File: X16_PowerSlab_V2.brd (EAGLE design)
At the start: 152.4 x 76.2 mm, 45 parts, among them J1 CONN_796636-3, J2 CONN_796636-3, J3 CONN_ET60T

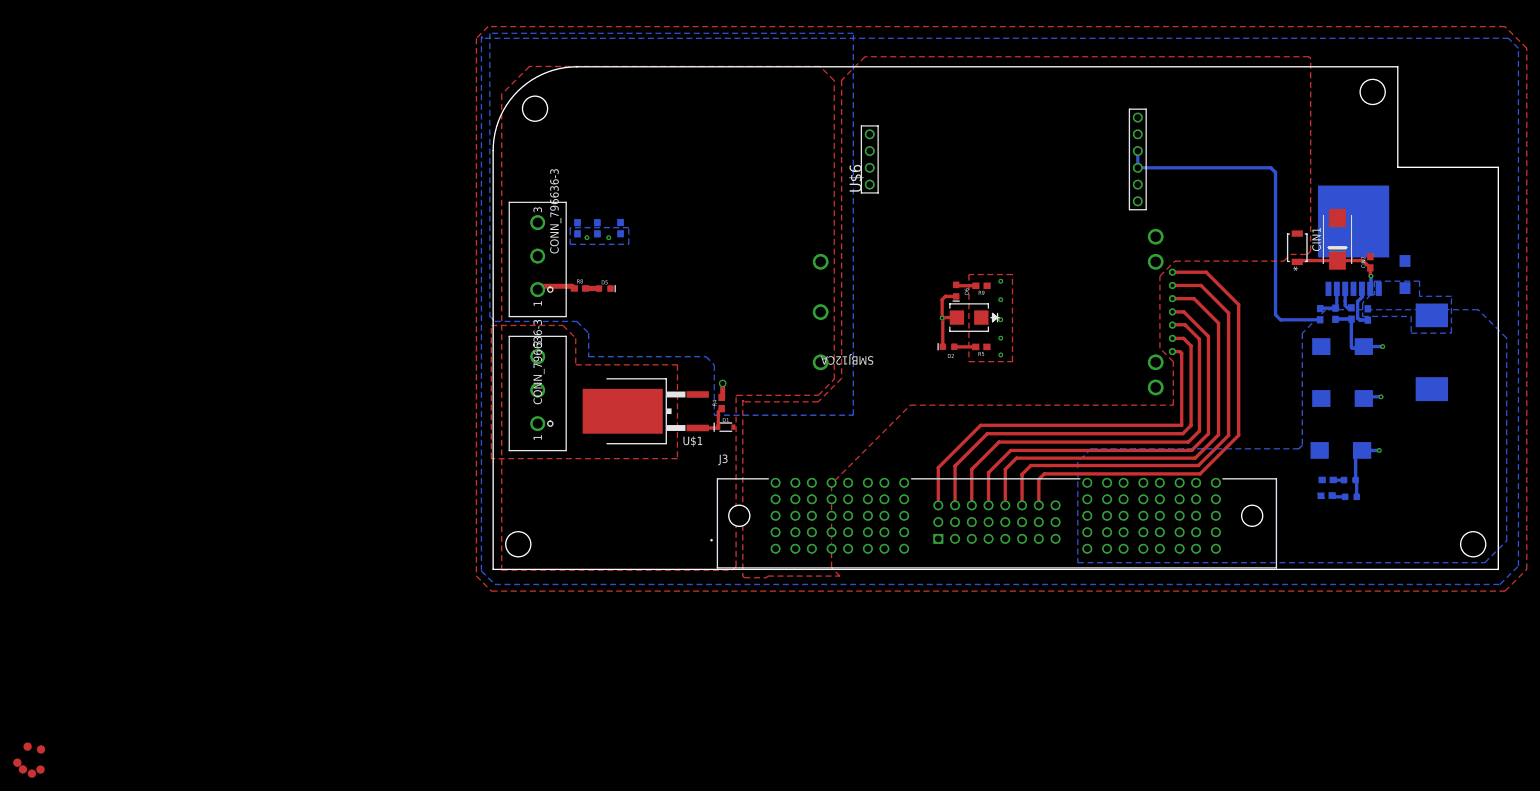
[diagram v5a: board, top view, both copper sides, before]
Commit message: Followed video, few discrepancies
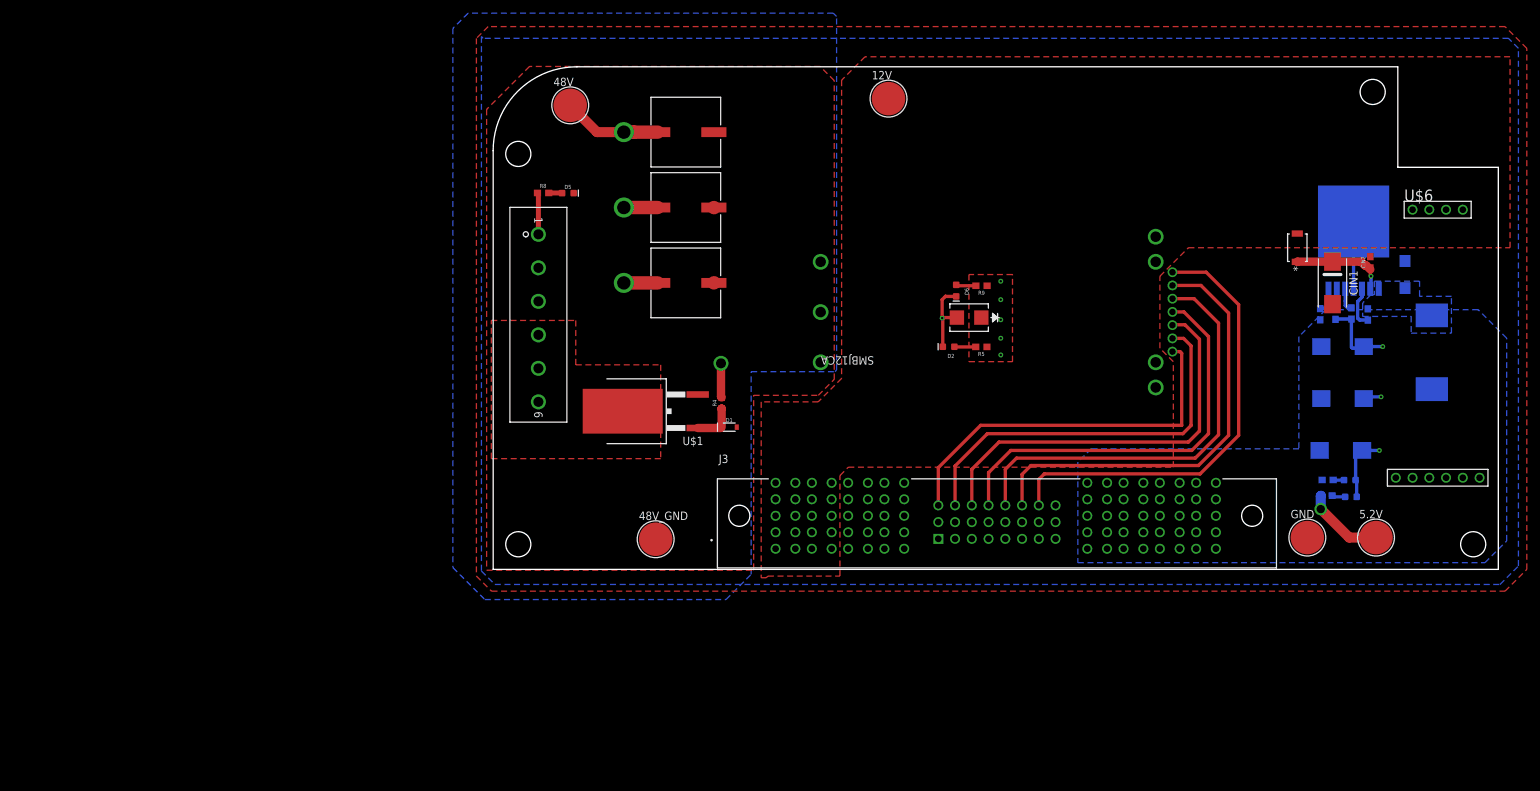
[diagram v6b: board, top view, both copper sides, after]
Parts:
- removed 12VGND_TP, 12V_TP, 48VGND_TP, 48_TP, TP5, TP6: TEST-POINT3X5, SparkFun-Connectors:PAD.03X.05
- removed C3, C4, C7: 330uF, SparkFun-Capacitors:0603-POLAR
- removed J1, J2: CONN_796636-3, X16_Power_Slab:CONN_796636-3
- added 12V, 48V_GND, 5.2V, GND: TESTPOINT_5.04MM, X16-ExtraComponents:TESTPOINT_5.04MM
- added 48V: 48V, X16-ExtraComponents:TESTPOINT_5.04MM
- added C1, C5, C6: UCM1H331MNL1GS, X16_Power_Slab:CAP_UCD_10X10_NCH
- added J4: 796636-6, X16_Power_Slab:CON6_P5MM_VER_TERM-BLK_TYC
- D1: value 15V -> 3.6V
- R1: value 1k -> (none)
- R10: value 100 -> 0.1
- R2: value 3.32k -> (none)
- R4: value 1M -> (none)
- R5: value 600 -> (none)
- R6: value 300 -> (none)
- R8: value 1.5k -> 0.1
- R9: value 470 -> 0.1
- RADJ: value 12.4k -> (none)
- moved U$6 71.5 mm to (143.2, 34.2), turned to 0 degrees
- moved D5 15.5 mm to (11.3, 57.0)
- moved R8 15.5 mm to (7.57, 57.1)
- moved H2 7.31 mm to (3.81, 63.0)
- moved CIN1 6.65 mm to (127.3, 43.4), turned to 270 degrees
- moved D1 0.51 mm to (35.8, 21.6)
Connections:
- net 12V: now also 12V.TP, J3.08, J3.16, J3.24
- net 48V: now also 48V.TP, C1.1, C5.1, C6.1, J4.1, J4.2, J4.3; no longer C3.+, C4.+, C7.+, J1.1, J1.2, J1.3
- net 48V_GND: now also 48V_GND.TP, C1.2, C5.2, C6.2; no longer C3.-, C4.-, C7.-
- net 5.2V: now also 5.2V.TP
- net GND: now also GND.TP
- net GND_RAW: now also J4.4, J4.5, J4.6; no longer J2.1, J2.2, J2.3
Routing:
- net 5.2V: track 52.4 -> 12.2 mm, vias 0 -> 1
- net 48V: track 8.16 -> 38.3 mm, vias 1 -> 4
- net GND: track 36.2 -> 46.4 mm
- net 48V_GND: track 0.00 -> 0.07 mm, vias 2 -> 0
- removed copper zone on layer 16, net 48V_GND

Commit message: Board finished; ran DRC
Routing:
- net 12V: track 0.00 -> 84.9 mm
- net GND: track 46.4 -> 51.8 mm, vias 4 -> 5
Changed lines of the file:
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@@
 <wire x1="130.4544" y1="42.545" x2="130.4544" y2="52.74" width="0.508" layer="16"/>
 <contactref element="GND" pad="TP"/>
+<wire x1="127.254" y1="40.214" x2="122.092" y2="40.214" width="1.016" layer="1"/>
+<wire x1="122.092" y1="40.214" x2="121.92" y2="40.386" width="1.016" layer="1"/>
+<via x="121.92" y="40.386" extent="1-16" drill="1.27"/>
 </signal>
 <signal name="N$1">
@@
 <contactref element="C5" pad="2"/>
 <contactref element="C1" pad="2"/>
-<wire x1="33.4645" y1="43.434" x2="33.48990625" y2="43.45940625" width="2.032" layer="1"/>
-<wire x1="33.4645" y1="54.864" x2="33.4899" y2="54.8386" width="2.032" layer="1"/>
 <contactref element="48V_GND" pad="TP"/>
-<wire x1="33.48990625" y1="43.45940625" x2="49.653" y2="46.632" width="0" layer="19" extent="1-1"/>
-<wire x1="33.4899" y1="54.8386" x2="33.48990625" y2="43.45940625" width="0" layer="19" extent="1-1"/>
-<wire x1="33.4645" y1="66.294" x2="33.4645" y2="54.864" width="0" layer="19" extent="1-1"/>
 </signal>
 <signal name="N$7">
@@
 <contactref element="R10" pad="2"/>
 <contactref element="D7" pad="A"/>
-<wire x1="129.171" y1="11.05493125" x2="129.171" y2="10.9982" width="0.762" layer="16"/>
 <wire x1="127.21498125" y1="11.18193125" x2="127.3987125" y2="10.9982" width="0.508" layer="16"/>
 <wire x1="127.3987125" y1="10.9982" x2="129.171" y2="10.9982" width="0.508" layer="16"/>
@@
 <contactref element="J3" pad="16"/>
 <contactref element="12V" pad="TP"/>
-<wire x1="85.27" y1="7.168" x2="85.27" y2="9.708" width="0" layer="19" extent="1-1"/>
-<wire x1="85.27" y1="4.628" x2="85.27" y2="7.168" width="0" layer="19" extent="1-1"/>
-<wire x1="100.453" y1="27.582" x2="85.27" y2="9.708" width="0" layer="19" extent="1-1"/>
+<wire x1="85.27" y1="4.628" x2="85.27" y2="3.104" width="1.016" layer="1"/>
+<wire x1="85.27" y1="3.104" x2="84.452" y2="2.286" width="1.016" layer="1"/>
+<wire x1="84.452" y1="2.286" x2="66.294" y2="2.286" width="1.016" layer="1"/>
+<wire x1="66.294" y1="2.286" x2="65.024" y2="3.556" width="1.016" layer="1"/>
+<wire x1="68.984" y1="27.582" x2="100.453" y2="27.582" width="1.016" layer="1"/>
+<wire x1="65.024" y1="3.556" x2="65.024" y2="23.622" width="1.016" layer="1"/>
+<wire x1="65.024" y1="23.622" x2="68.984" y2="27.582" width="1.016" layer="1"/>
+<wire x1="85.27" y1="9.708" x2="85.27" y2="7.168" width="1.016" layer="1"/>
+<wire x1="85.27" y1="7.168" x2="85.27" y2="4.628" width="1.016" layer="1"/>
 </signal>
 <signal name="5.2V">
@@
 <contactref element="CIN1" pad="+"/>
 <contactref element="CR2" pad="1"/>
-<wire x1="121.92" y1="46.6217" x2="122.1163" y2="46.818" width="0.508" layer="1"/>
 <wire x1="132.9944" y1="45.7082" x2="132.9944" y2="45.466" width="0.508" layer="1"/>
 <wire x1="132.9944" y1="45.466" x2="132.9944" y2="44.5516" width="0.508" layer="1"/>

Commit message: Labels added
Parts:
- D2, D3, D5, D6, D7: device SparkFun-LED:LED-0603 -> SparkFun-LED:LED-0805
- renumbered 12V to 12V_TP, 48V to 48V_TP, 48V_GND to 48V_GND_TP, 5.2V to 5.2V_TP, CR1 to BACK_EMF, DIODE to 40V_DIODE, GND to GND_TP, J3 to BACKPLANE_CONN, U$1 to TRANS_REVERSE_VOLT_PROTEC, U$3 to BMR480_POWERBRICK
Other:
- board text added: "12V"
- board text added: "48V"
- board text added: "5.2V"
- board text added: "BACK_EMF_DIODE"
- board text added: "BMR480_PWRBRICK"
- board text added: "BUCK_CONVERTER"
- board text added: "C1"
- board text added: "C5"
- board text added: "C6"
- board text added: "GND"
- board text added: "GND_RAW"
- board text added: "L1"
- board text added: "PMBUS"
- board text added: "TETHER_CONN"
- board text added: "X16 Power Slab Minh, Raghav, Vijay, Daniel Rhea Virk"
